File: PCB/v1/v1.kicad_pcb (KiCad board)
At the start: 2 copper layers, 36 parts, among them J1 Screw_Terminal_01x02, Q2 BC548, SW1 Push Button, SW2 Push Button, U1 4060, U10 7400, U2 4060, U3 CD4026BE, U4 CD4026BE, U5 CD4026BE, U6 CD4026BE, U7 CD4026BE, U8 CD4026BE, Y1 32.768kHz

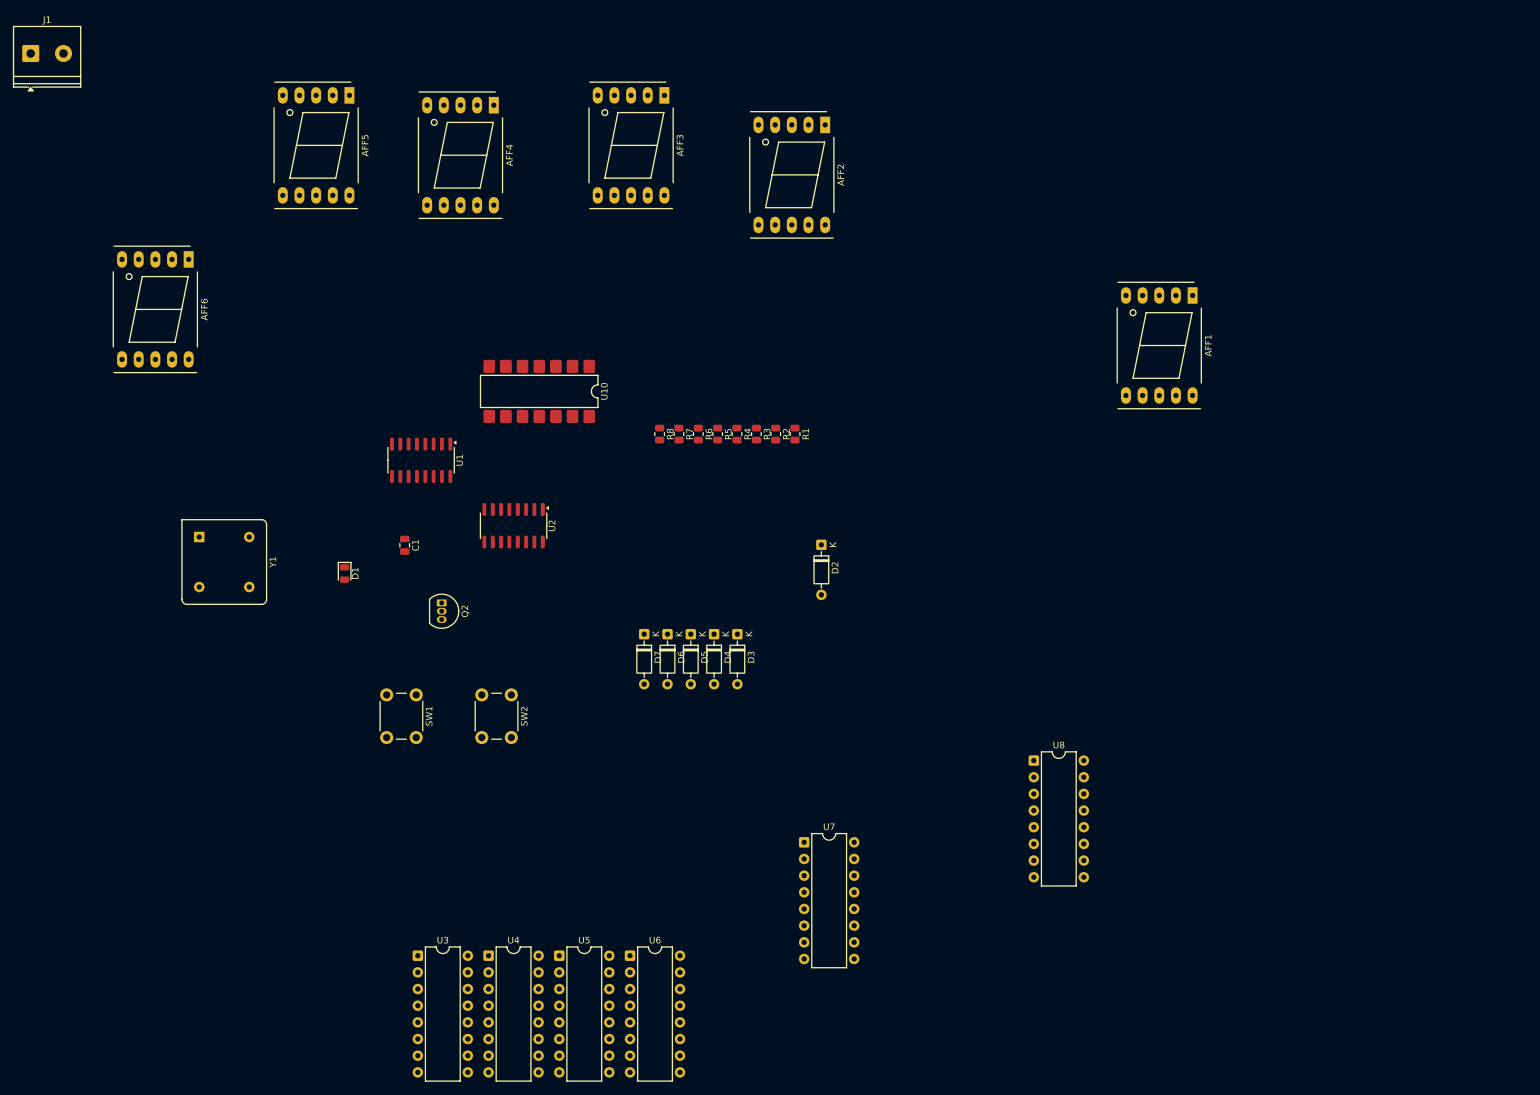
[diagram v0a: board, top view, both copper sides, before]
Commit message: Updated Schematic, made PCB Design
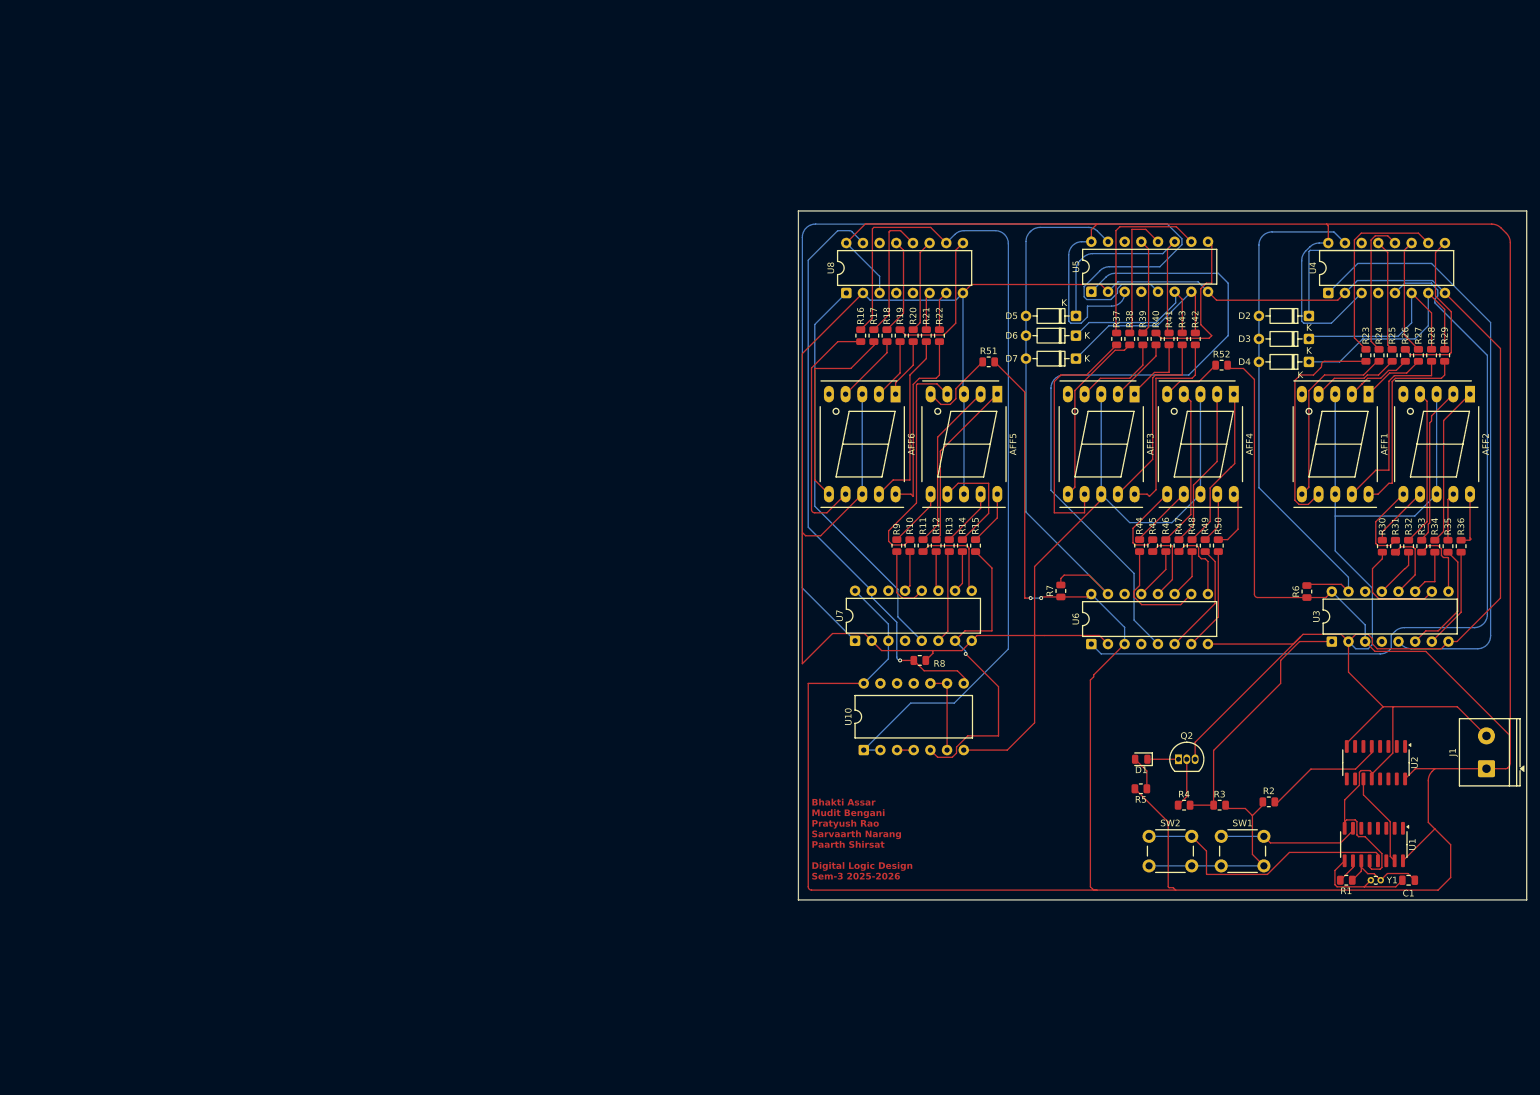
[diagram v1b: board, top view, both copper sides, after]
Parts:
- added R10: 330R, Resistor_SMD:R_0805_2012Metric, F.Cu at (159.0, 100.5)
- added R11: 330R, Resistor_SMD:R_0805_2012Metric, F.Cu at (161.0, 100.5)
- added R12: 330R, Resistor_SMD:R_0805_2012Metric, F.Cu at (163.0, 100.5)
- added R13: 330R, Resistor_SMD:R_0805_2012Metric, F.Cu at (165.0, 100.5)
- added R14: 330R, Resistor_SMD:R_0805_2012Metric, F.Cu at (167.0, 100.5)
- added R15: 330R, Resistor_SMD:R_0805_2012Metric, F.Cu at (169.0, 100.5)
- added R16: 330R, Resistor_SMD:R_0805_2012Metric, F.Cu at (151.5, 68.5)
- added R17: 330R, Resistor_SMD:R_0805_2012Metric, F.Cu at (153.5, 68.5)
- added R18: 330R, Resistor_SMD:R_0805_2012Metric, F.Cu at (155.5, 68.5)
- added R19: 330R, Resistor_SMD:R_0805_2012Metric, F.Cu at (157.5, 68.5)
- added R20: 330R, Resistor_SMD:R_0805_2012Metric, F.Cu at (159.5, 68.5)
- added R21: 330R, Resistor_SMD:R_0805_2012Metric, F.Cu at (161.5, 68.5)
- added R22: 330R, Resistor_SMD:R_0805_2012Metric, F.Cu at (163.5, 68.5)
- added R23: 330R, Resistor_SMD:R_0805_2012Metric, F.Cu at (228.5, 71.5)
- added R24: 330R, Resistor_SMD:R_0805_2012Metric, F.Cu at (230.5, 71.5)
- added R25: 330R, Resistor_SMD:R_0805_2012Metric, F.Cu at (232.5, 71.5)
- added R26: 330R, Resistor_SMD:R_0805_2012Metric, F.Cu at (234.5, 71.5)
- added R27: 330R, Resistor_SMD:R_0805_2012Metric, F.Cu at (236.5, 71.5)
- added R28: 330R, Resistor_SMD:R_0805_2012Metric, F.Cu at (238.5, 71.5)
- added R29: 330R, Resistor_SMD:R_0805_2012Metric, F.Cu at (240.5, 71.5)
- added R30: 330R, Resistor_SMD:R_0805_2012Metric, F.Cu at (231.0, 100.6)
- added R31: 330R, Resistor_SMD:R_0805_2012Metric, F.Cu at (233.0, 100.6)
- added R32: 330R, Resistor_SMD:R_0805_2012Metric, F.Cu at (235.0, 100.6)
- added R33: 330R, Resistor_SMD:R_0805_2012Metric, F.Cu at (237.0, 100.6)
- added R34: 330R, Resistor_SMD:R_0805_2012Metric, F.Cu at (239.0, 100.6)
- added R35: 330R, Resistor_SMD:R_0805_2012Metric, F.Cu at (241.0, 100.6)
- added R36: 330R, Resistor_SMD:R_0805_2012Metric, F.Cu at (243.0, 100.6)
- added R37: 330R, Resistor_SMD:R_0805_2012Metric, F.Cu at (190.5, 69.0)
- added R38: 330R, Resistor_SMD:R_0805_2012Metric, F.Cu at (192.5, 69.0)
- added R39: 330R, Resistor_SMD:R_0805_2012Metric, F.Cu at (194.5, 69.0)
- added R40: 330R, Resistor_SMD:R_0805_2012Metric, F.Cu at (196.5, 69.0)
- added R41: 330R, Resistor_SMD:R_0805_2012Metric, F.Cu at (198.5, 69.0)
- added R42: 330R, Resistor_SMD:R_0805_2012Metric, F.Cu at (200.5, 69.0)
- added R43: 330R, Resistor_SMD:R_0805_2012Metric, F.Cu at (202.5, 69.0)
- added R44: 330R, Resistor_SMD:R_0805_2012Metric, F.Cu at (194.0, 100.5)
- added R45: 330R, Resistor_SMD:R_0805_2012Metric, F.Cu at (196.0, 100.5)
- added R46: 330R, Resistor_SMD:R_0805_2012Metric, F.Cu at (198.0, 100.5)
- added R47: 330R, Resistor_SMD:R_0805_2012Metric, F.Cu at (200.0, 100.5)
- added R48: 330R, Resistor_SMD:R_0805_2012Metric, F.Cu at (202.0, 100.5)
- added R49: 330R, Resistor_SMD:R_0805_2012Metric, F.Cu at (204.0, 100.5)
- added R50: 330R, Resistor_SMD:R_0805_2012Metric, F.Cu at (206.0, 100.5)
- added R51: 330R, Resistor_SMD:R_0805_2012Metric, F.Cu at (171.0, 72.5)
- added R52: 330R, Resistor_SMD:R_0805_2012Metric, F.Cu at (206.5, 73.0)
- added R9: 330R, Resistor_SMD:R_0805_2012Metric, F.Cu at (157.0, 100.5)
- R5: value 330 -> 330R
- U10: footprint Package_DIP:SMDIP-14_W7.62mm -> Package_DIP:DIP-14_W10.16mm
- Y1: footprint Oscillator:Oscillator_DIP-8 -> Crystal:Crystal_DS10_D1.0mm_L4.3mm_Vertical
- moved J1 247.2 mm to (246.9, 134.5), turned to 90 degrees
- moved Y1 186.1 mm to (229.2, 151.5), turned to 0 degrees
- moved U4 163.0 mm to (222.8, 62.0), turned to 90 degrees
- moved C1 161.3 mm to (235.0, 151.5), turned to 0 degrees
- moved U1 156.6 mm to (229.7, 146.1)
- moved U3 147.3 mm to (223.3, 115.1), turned to 90 degrees
- moved U2 136.3 mm to (230.0, 133.6)
- moved U5 129.7 mm to (186.7, 61.8), turned to 90 degrees
- moved D1 124.7 mm to (194.3, 133.1), turned to 180 degrees
- moved SW1 124.6 mm to (206.4, 144.8), turned to 0 degrees
- moved AFF4 121.1 mm to (208.4, 77.4)
- moved Q2 114.8 mm to (199.9, 133.1), turned to 0 degrees
- moved AFF6 109.7 mm to (156.8, 77.4)
- moved AFF5 108.7 mm to (172.3, 77.4)
- moved R1 108.1 mm to (225.5, 151.5), turned to 180 degrees
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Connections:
- net Net-(U4-CARRY_OUT) renamed /CLK - Mod-60 (2)
- net Net-(U5-CARRY_OUT) renamed /CLK - Mod-12
- AFF4 pad 5: unconnected-(AFF4-DP-Pad5) -> Net-(AFF4-DP)
- AFF5 pad 5: unconnected-(AFF5-DP-Pad5) -> Net-(AFF5-DP)
- D2 pad 1: Net-(AFF2-e) -> Net-(D2-K)
- D3 pad 1: Net-(AFF2-f) -> Net-(D3-K)
- D4 pad 1: Net-(AFF2-g) -> Net-(D4-K)
- D5 pad 1: Net-(AFF4-e) -> Net-(D5-K)
- D6 pad 1: Net-(AFF4-f) -> Net-(D6-K)
- D7 pad 1: Net-(AFF4-g) -> Net-(D7-K)
- R3 pad 1: Net-(R3-Pad1) -> /CLK - Mod-60 (1)
- R4 pad 2: Net-(R3-Pad1) -> /CLK - Mod-60 (1)
- R6 pad 1: unconnected-(R6-Pad1) -> +6V
- U10 pad 1: Net-(AFF6-a) -> Net-(U8-A)
- U10 pad 2: Net-(AFF6-a) -> Net-(U8-A)
- U10 pad 5: Net-(AFF5-g) -> Net-(U7-G)
- U3 pad 1: Net-(D1-K) -> /CLK - Mod-60 (1)
- U3 pad 10: Net-(AFF2-a) -> Net-(U3-A)
- U3 pad 11: Net-(AFF2-e) -> Net-(U3-E)
- U3 pad 12: Net-(AFF2-b) -> Net-(U3-B)
- U3 pad 13: Net-(AFF2-c) -> Net-(U3-C)
- U3 pad 6: Net-(AFF2-f) -> Net-(U3-F)
- U3 pad 7: Net-(AFF2-g) -> Net-(U3-G)
- U3 pad 9: Net-(AFF2-d) -> Net-(U3-D)
- U4 pad 10: Net-(AFF1-a) -> Net-(U4-A)
- U4 pad 11: Net-(AFF1-e) -> Net-(D2-K)
- U4 pad 12: Net-(AFF1-b) -> Net-(U4-B)
- U4 pad 13: Net-(AFF1-c) -> Net-(U4-C)
- U4 pad 6: Net-(AFF1-f) -> Net-(D3-K)
- U4 pad 7: Net-(AFF1-g) -> Net-(D4-K)
- U4 pad 9: Net-(AFF1-d) -> Net-(U4-D)
- U5 pad 10: Net-(AFF3-a) -> Net-(U5-A)
- U5 pad 11: Net-(AFF3-e) -> Net-(D5-K)
- U5 pad 12: Net-(AFF3-b) -> Net-(U5-B)
- U5 pad 13: Net-(AFF3-c) -> Net-(U5-C)
- U5 pad 6: Net-(AFF3-f) -> Net-(D6-K)
- U5 pad 7: Net-(AFF3-g) -> Net-(D7-K)
- U5 pad 9: Net-(AFF3-d) -> Net-(U5-D)
- U6 pad 10: Net-(AFF4-a) -> Net-(U6-A)
- U6 pad 11: Net-(AFF4-e) -> Net-(U6-E)
- U6 pad 12: Net-(AFF4-b) -> Net-(U6-B)
- U6 pad 13: Net-(AFF4-c) -> Net-(U6-C)
- U6 pad 6: Net-(AFF4-f) -> Net-(U6-F)
- U6 pad 7: Net-(AFF4-g) -> Net-(U6-G)
- U6 pad 9: Net-(AFF4-d) -> Net-(U6-D)
- U7 pad 10: Net-(AFF5-a) -> Net-(U7-A)
- U7 pad 11: Net-(AFF5-e) -> Net-(U7-E)
- U7 pad 12: Net-(AFF5-b) -> Net-(U7-B)
- U7 pad 13: Net-(AFF5-c) -> Net-(U7-C)
- U7 pad 6: Net-(AFF5-f) -> Net-(U7-F)
- U7 pad 7: Net-(AFF5-g) -> Net-(U7-G)
- U7 pad 9: Net-(AFF5-d) -> Net-(U7-D)
- U8 pad 10: Net-(AFF6-a) -> Net-(U8-A)
- U8 pad 11: Net-(AFF6-e) -> Net-(U8-E)
- U8 pad 12: Net-(AFF6-b) -> Net-(U8-B)
- U8 pad 13: Net-(AFF6-c) -> Net-(U8-C)
- U8 pad 6: Net-(AFF6-f) -> Net-(U8-F)
- U8 pad 7: Net-(AFF6-g) -> Net-(U8-G)
- U8 pad 9: Net-(AFF6-d) -> Net-(U8-D)
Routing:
- net +6V: track 0.00 -> 658.8 mm, vias 0 -> 2
- net GND: track 0.00 -> 649.5 mm
- net /CLK - Mod-12: track 0.00 -> 158.5 mm
- net Net-(U8-A): track 0.00 -> 132.4 mm
- net /CLK - Mod-60 (2): track 0.00 -> 125.3 mm
- net Net-(U5-CLK): track 0.00 -> 106.8 mm
- net Net-(U3-CARRY_OUT): track 0.00 -> 93.5 mm
- net Net-(U7-RESET): track 0.00 -> 89.1 mm, vias 0 -> 1
- net Net-(D5-A): track 0.00 -> 83.0 mm
- net Net-(D2-A): track 0.00 -> 80.2 mm
- net Net-(U7-CARRY_OUT): track 0.00 -> 61.7 mm
- net Net-(U7-G): track 0.00 -> 49.3 mm, vias 0 -> 1
- net Net-(D2-K): track 0.00 -> 44.3 mm
- net Net-(U1-Q9): track 0.00 -> 41.8 mm
- net Net-(AFF3-a): track 0.00 -> 39.3 mm
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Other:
- board outline added: 111 x 105 mm
- board text added: "Bhakti Assar Mudit Bengani Pratyush Rao Sarvaarth Narang Paarth Shirsat Digital Logic Design Sem-3 2025-2026"

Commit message: Updated Schematic
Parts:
- added C10: 0.1u, Capacitor_SMD:C_0805_2012Metric_Pad1.18x1.45mm_HandSolder, F.Cu at (93.8, 66.8)
- added C2: 0.1u, Capacitor_SMD:C_0805_2012Metric_Pad1.18x1.45mm_HandSolder, F.Cu at (166.0, 77.8)
- added C3: 0.1u, Capacitor_SMD:C_0805_2012Metric_Pad1.18x1.45mm_HandSolder, F.Cu at (82.8, 98.0)
- added C4: 0.1u, Capacitor_SMD:C_0805_2012Metric_Pad1.18x1.45mm_HandSolder, F.Cu at (157.2, 78.8)
- added C5: 0.1u, Capacitor_SMD:C_0805_2012Metric_Pad1.18x1.45mm_HandSolder, F.Cu at (60.0, 96.2)
- added C6: 0.1u, Capacitor_SMD:C_0805_2012Metric_Pad1.18x1.45mm_HandSolder, F.Cu at (68.0, 65.0)
- added C7: 0.1u, Capacitor_SMD:C_0805_2012Metric_Pad1.18x1.45mm_HandSolder, F.Cu at (166.0, 67.8)
- added C8: 0.1u, Capacitor_SMD:C_0805_2012Metric_Pad1.18x1.45mm_HandSolder, F.Cu at (104.2, 97.8)
- added C9: 0.1u, Capacitor_SMD:C_0805_2012Metric_Pad1.18x1.45mm_HandSolder, F.Cu at (120.0, 68.0)
- moved D4 168.5 mm to (53.5, 99.9), turned to 90 degrees
- moved D2 167.1 mm to (56.2, 99.9), turned to 90 degrees
- moved D3 164.9 mm to (56.2, 89.6), turned to 90 degrees
- moved D5 133.0 mm to (53.5, 89.6), turned to 90 degrees
- moved D7 131.0 mm to (53.5, 79.6), turned to 90 degrees
- moved D6 128.5 mm to (56.2, 79.6), turned to 90 degrees
- moved U3 119.9 mm to (103.6, 107.8)
- moved AFF2 110.8 mm to (134.8, 94.2), turned to 90 degrees
- moved R15 109.3 mm to (59.9, 94.0), turned to 180 degrees
- moved AFF1 109.3 mm to (120.9, 94.2), turned to 90 degrees
- moved R43 108.6 mm to (93.9, 72.0), turned to 0 degrees
- moved R14 107.4 mm to (59.9, 92.0), turned to 180 degrees
- moved R40 106.9 mm to (89.6, 66.8), turned to 0 degrees
- moved R42 106.7 mm to (93.9, 74.0), turned to 0 degrees
- moved R30 106.4 mm to (124.8, 105.3)
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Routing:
- net +6V: track 658.8 -> 316.9 mm, vias 2 -> 0
- net GND: track 649.5 -> 361.0 mm, vias 0 -> 1
- net Net-(D4-K): track 35.1 -> 141.5 mm, vias 0 -> 4
- net Net-(D2-A): track 80.2 -> 166.1 mm, vias 0 -> 1
- net Net-(D2-K): track 44.3 -> 129.7 mm, vias 0 -> 5
- net Net-(D3-K): track 31.1 -> 111.6 mm, vias 0 -> 4
- net Net-(D5-A): track 83.0 -> 163.2 mm, vias 0 -> 4
- net /CLK - Mod-12: track 158.5 -> 80.1 mm, vias 0 -> 1
- net Net-(U5-CLK): track 106.8 -> 33.0 mm
- net Net-(AFF5-DP): track 12.2 -> 77.1 mm, vias 0 -> 3
- net Net-(U7-G): track 49.3 -> 109.2 mm
- net Net-(U7-RESET): track 89.1 -> 145.8 mm, vias 1 -> 4
- net Net-(U3-CARRY_OUT): track 93.5 -> 42.4 mm, vias 0 -> 3
- net Net-(U1-~{Φ1}): track 14.3 -> 64.9 mm, vias 0 -> 1
- net Net-(D7-K): track 28.3 -> 74.2 mm, vias 0 -> 1
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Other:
- board size 111 x 105 mm -> 126 x 47 mm
- board text added: "Made By Bhakti,Mudit,Pratyush Sarvaarth,Paarth DLD Sem 3 2025-2026"
- board text removed: "Bhakti Assar Mudit Bengani Pratyush Rao Sarvaarth Narang Paarth Shirsat Digital Logic Design Sem-3 2025-2026"

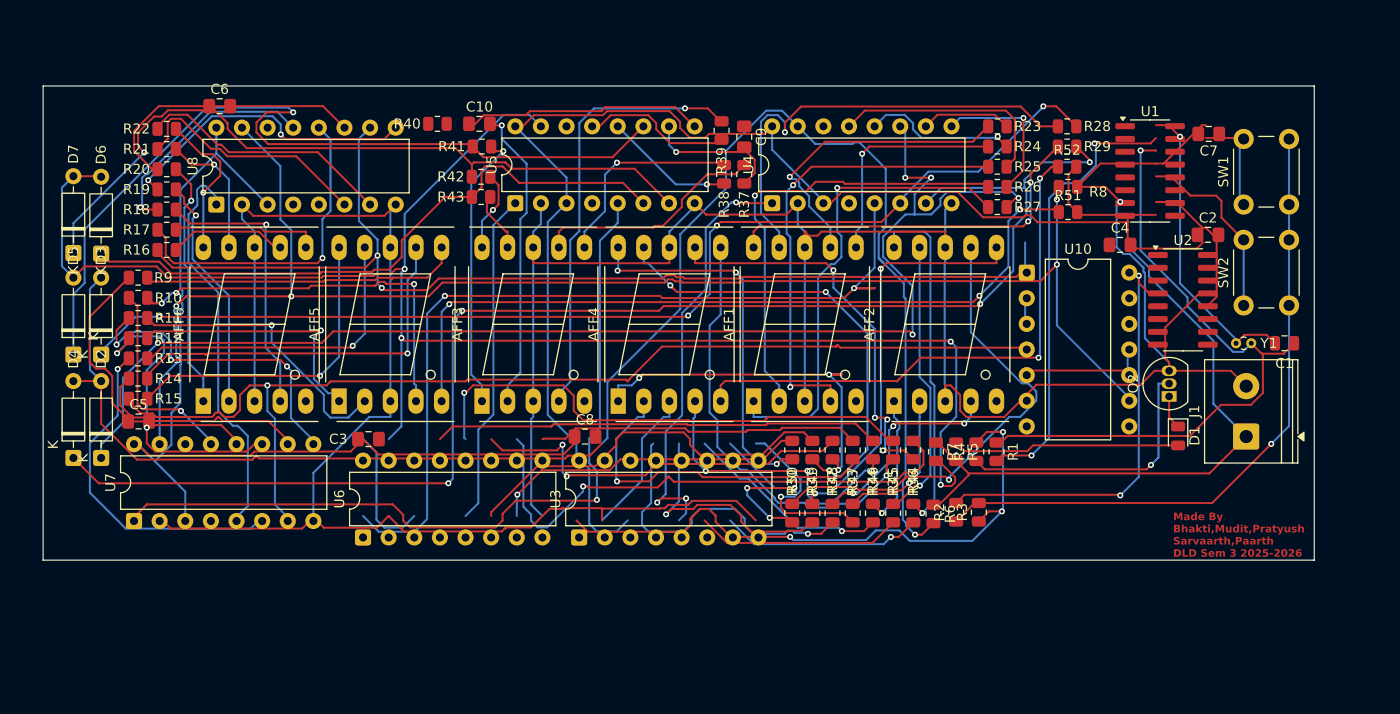
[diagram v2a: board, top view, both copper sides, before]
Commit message: PCB routed V5
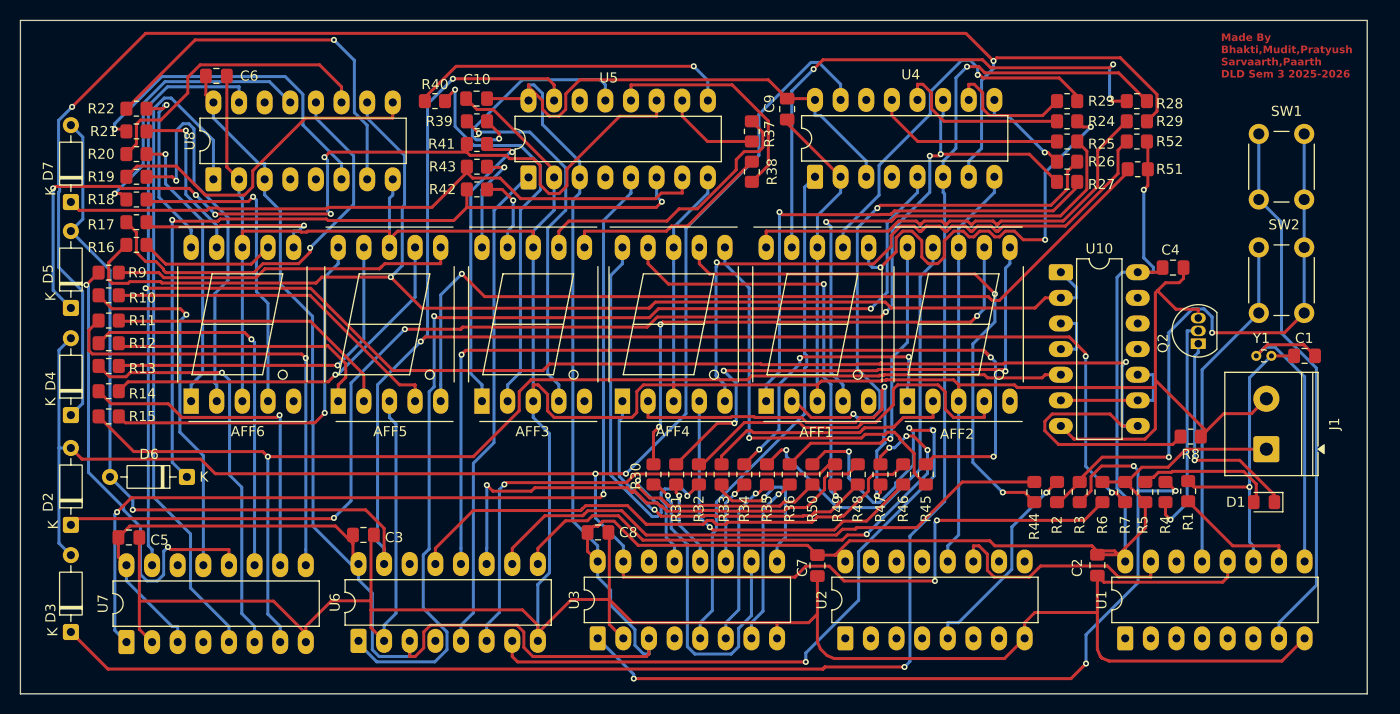
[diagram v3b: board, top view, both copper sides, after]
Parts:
- C1: footprint Capacitor_SMD:C_0805_2012Metric -> Capacitor_SMD:C_0805_2012Metric_Pad1.18x1.45mm_HandSolder
- D1: footprint LED_SMD:LED_0805_2012Metric -> LED_SMD:LED_0805_2012Metric_Pad1.15x1.40mm_HandSolder
- R1, R10, R11, R12, R13, R14, R15, R16, R17, R18, R19, R2, R20, R21, R22, R23, R24, R25, R26, R27, R28, R29, R3, R30, R31, R32, R33, R34, R35, R36, R37, R38, R39, R4, R40, R41, R42, R43, R44, R45, R46, R47, R48, R49, R5, R50, R51, R52, R6, R7, R8, R9: footprint Resistor_SMD:R_0805_2012Metric -> Resistor_SMD:R_0805_2012Metric_Pad1.20x1.40mm_HandSolder
- U1, U2: footprint Package_SO:SOIC-16_3.9x9.9mm_P1.27mm -> Package_DIP:DIP-16_W7.62mm_LongPads
- U10: footprint Package_DIP:DIP-14_W10.16mm -> Package_DIP:DIP-14_W7.62mm_LongPads
- U3, U4, U5, U6, U7, U8: footprint Package_DIP:DIP-16_W7.62mm -> Package_DIP:DIP-16_W7.62mm_LongPads
- moved C7 57.8 mm to (127.2, 110.5), turned to -90 degrees
- moved U2 47.4 mm to (130.0, 117.8), turned to 90 degrees
- moved U1 46.4 mm to (157.8, 117.8), turned to 90 degrees
- moved C2 34.5 mm to (155.0, 110.5), turned to -90 degrees
- moved D3 27.7 mm to (53.2, 117.1)
- moved R8 27.6 mm to (164.2, 97.8)
- moved R39 24.3 mm to (93.5, 66.5), turned to 180 degrees
- moved D6 23.7 mm to (64.8, 101.8), turned to 180 degrees
- moved R1 19.4 mm to (164.0, 103.2)
- moved R4 19.2 mm to (161.8, 103.2)
- moved R5 19.2 mm to (159.8, 103.2)
- moved R7 19.2 mm to (157.8, 103.2)
- moved R6 16.9 mm to (155.5, 103.2)
- moved R30 14.3 mm to (111.0, 101.5)
- moved R31 14.0 mm to (113.2, 101.5)
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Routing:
- net GND: track 361.0 -> 569.1 mm, vias 1 -> 0
- net +6V: track 316.9 -> 396.6 mm, vias 0 -> 1
- net Net-(D3-K): track 111.6 -> 166.0 mm, vias 4 -> 2
- net Net-(D5-A): track 163.2 -> 217.5 mm, vias 4 -> 5
- net Net-(U6-G): track 31.6 -> 82.0 mm, vias 1 -> 4
- net Net-(U7-RESET): track 145.8 -> 192.1 mm, vias 4 -> 2
- net Net-(U6-B): track 51.2 -> 94.5 mm, vias 1 -> 3
- net Net-(U1-Q4): track 10.6 -> 53.9 mm
- net Net-(U1-~{Φ1}): track 64.9 -> 30.0 mm
- net Net-(D2-A): track 166.1 -> 200.1 mm, vias 1 -> 4
- net Net-(U1-Φ0): track 44.4 -> 12.4 mm, vias 2 -> 0
- net Net-(U7-CARRY_OUT): track 39.6 -> 67.9 mm
- net /CLK - Mod-60 (1): track 61.3 -> 85.6 mm, vias 3 -> 4
- net Net-(U6-D): track 32.5 -> 54.4 mm, vias 0 -> 4
- net Net-(U2-Q5): track 41.8 -> 20.6 mm, vias 2 -> 1
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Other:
- board size 126 x 47 mm -> 133.5 x 66.8 mm

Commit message: PCB Routing In progress
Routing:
- net +6V: track 396.6 -> 393.8 mm
- net Net-(U8-D): track 33.7 -> 32.8 mm
- net Net-(U5-B): track 23.4 -> 22.4 mm
- net Net-(U7-B): track 46.1 -> 45.2 mm
